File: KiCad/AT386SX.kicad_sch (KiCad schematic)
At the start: 31 parts, among them Q3 2N3904, U2 74HC05, U7 Cx486SLC, U8 80387SX, U9 RC2016A5, X1 CPU_CLK, X2 FPU_CLK, Y1 14.31818MHz

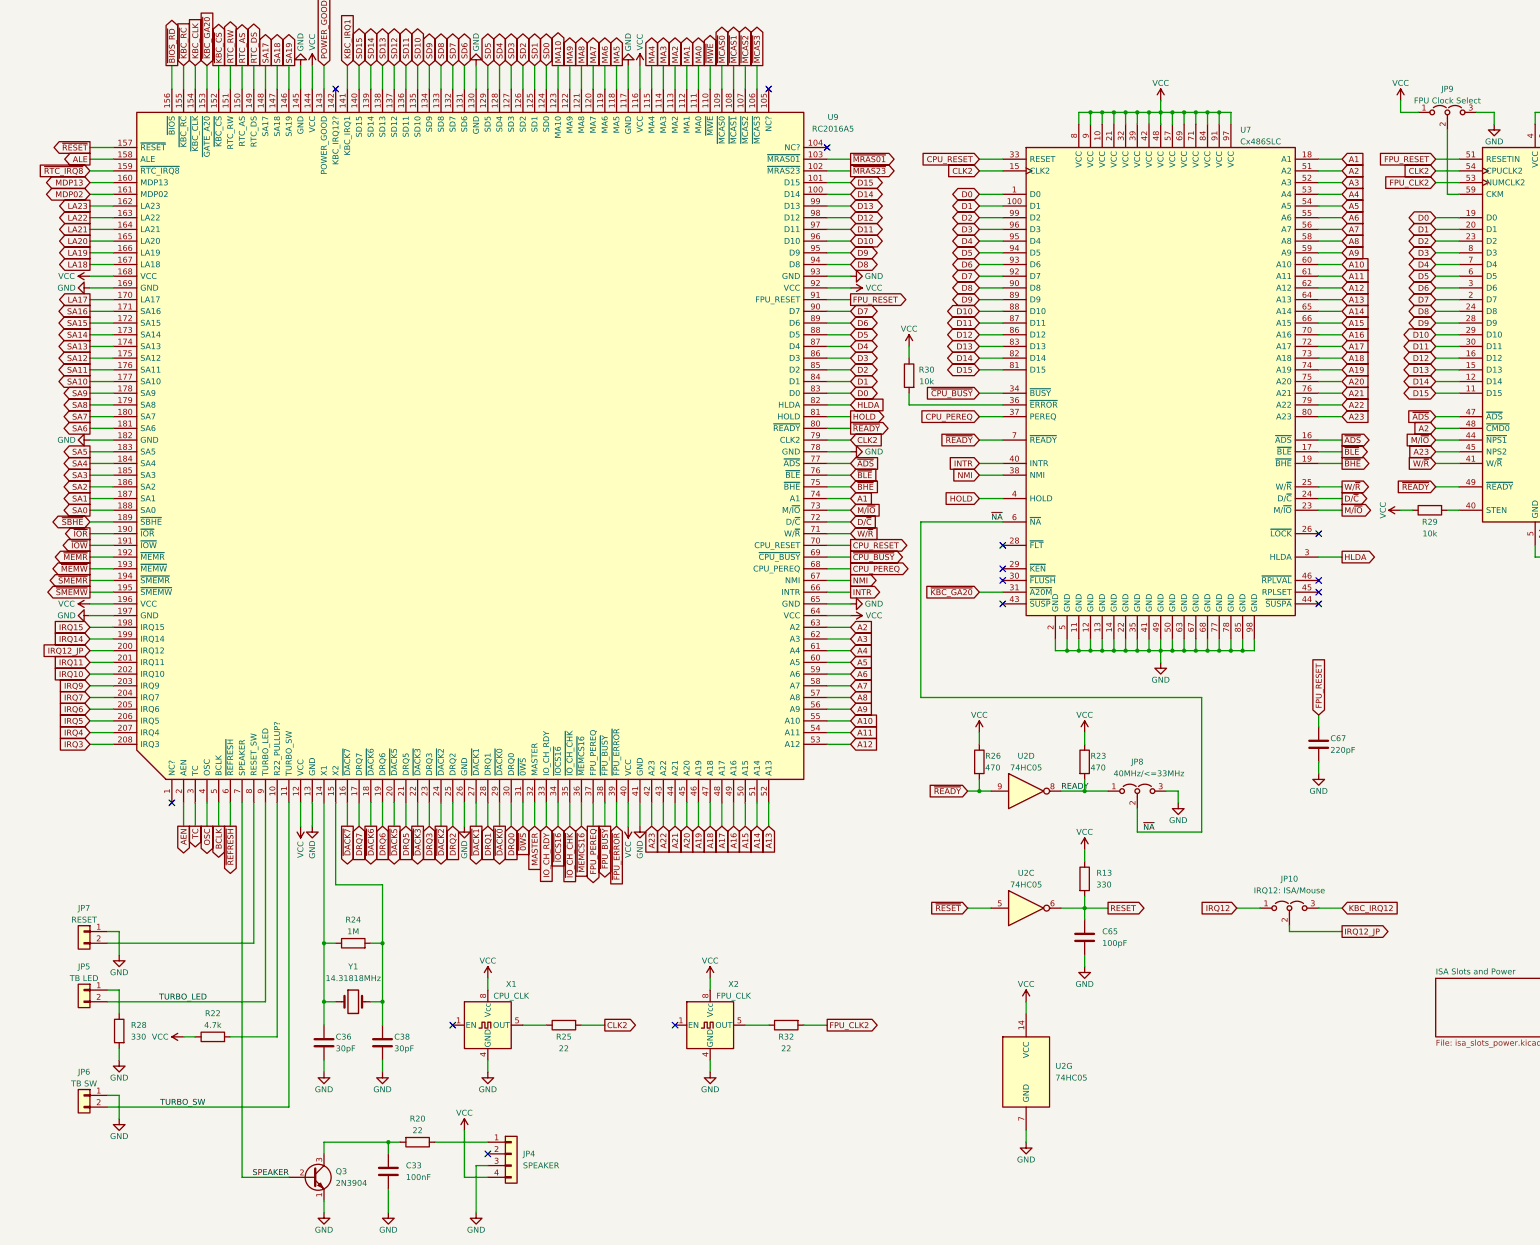
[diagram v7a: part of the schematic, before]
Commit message: Version 1.7: Use single front panel connector
Signed-off-by: Sergey Kiselev <skiselev@gmail.com>
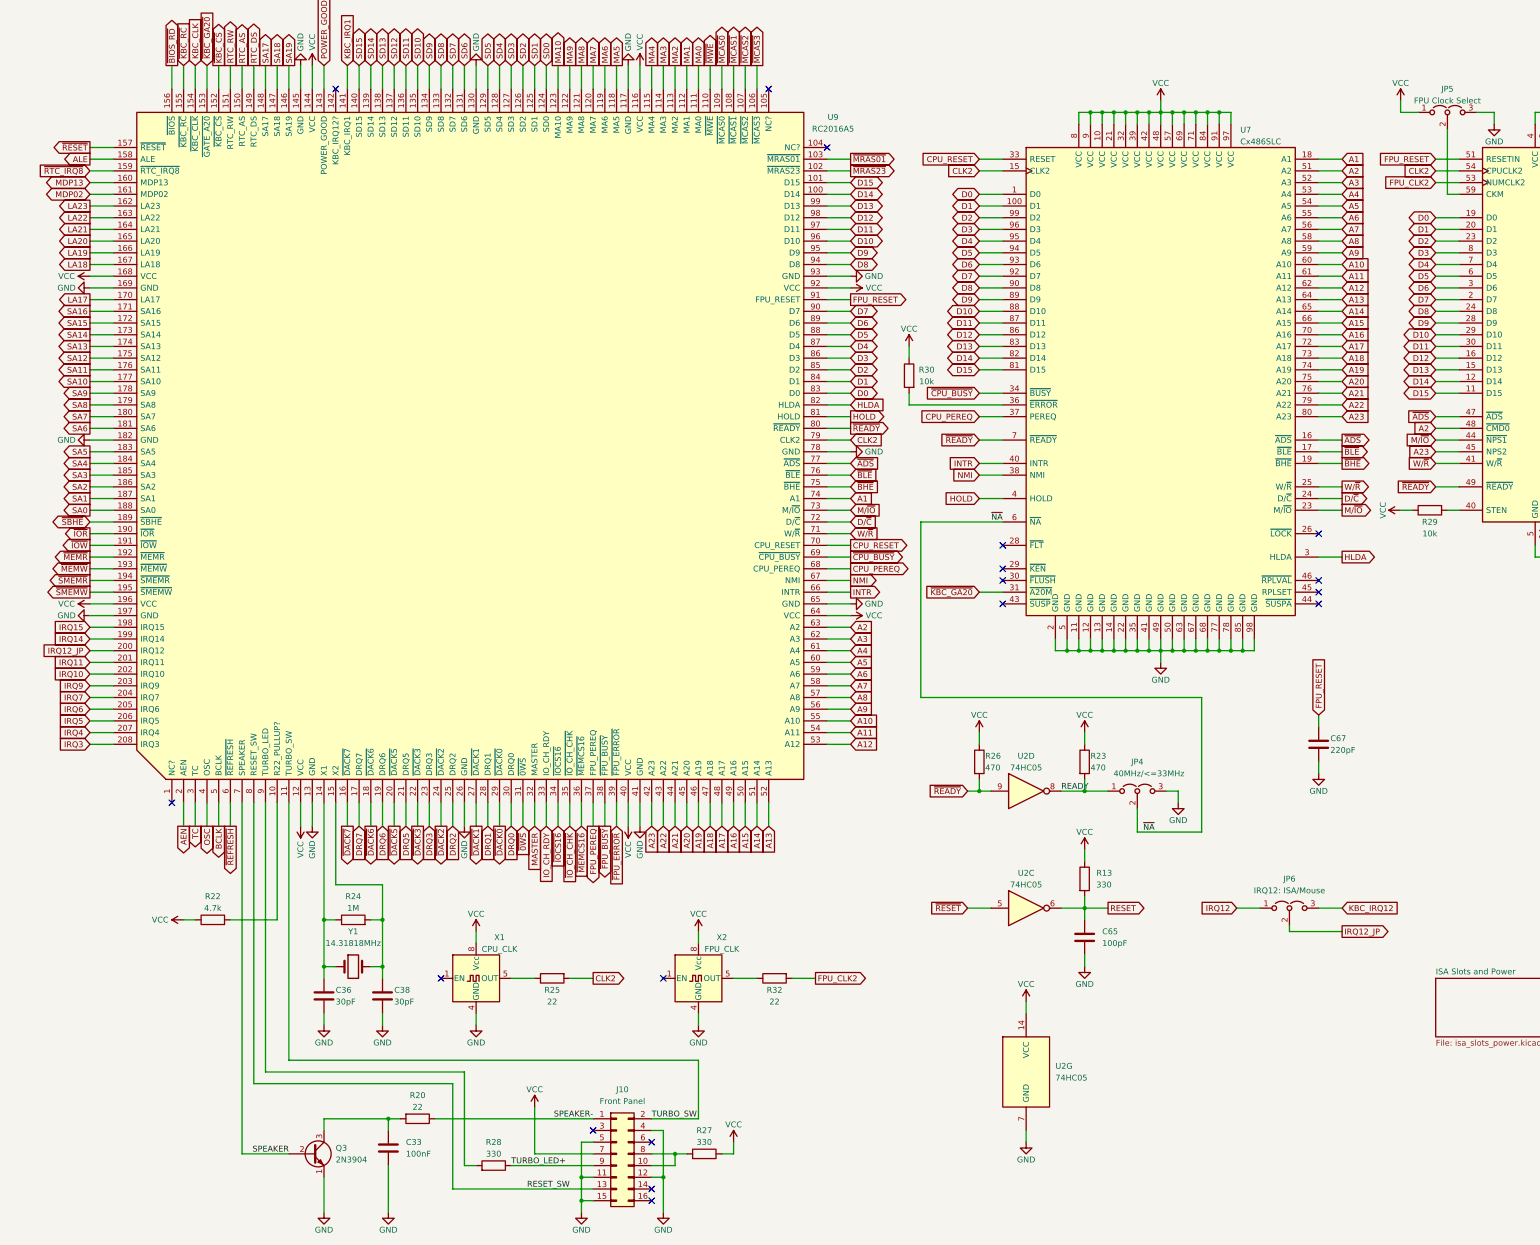
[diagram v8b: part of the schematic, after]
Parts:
- removed JP4: SPEAKER, My_Components:Conn_Pin_Header_4x1_2.54mm, symbol Connector_Generic:Conn_01x04
- removed JP5: TB LED, My_Components:Conn_Pin_Header_2x1_2.54mm, symbol Connector_Generic:Conn_01x02
- removed JP6: TB SW, My_Components:Conn_Pin_Header_2x1_2.54mm, symbol Connector_Generic:Conn_01x02
- removed JP7: RESET, My_Components:Conn_Pin_Header_2x1_2.54mm, symbol Connector_Generic:Conn_01x02
- added J10: Front Panel, My_Components:Conn_Pin_Header_8x2_2.54mm, symbol Connector_Generic:Conn_02x08_Odd_Even
- added R27: 330, My_Components:Res_762, symbol Device:R
- renumbered JP8 to JP4, JP9 to JP5, JP10 to JP6
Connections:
- net GND: now also J10.11 (Pin_11), J10.12 (Pin_12), J10.15 (Pin_15), J10.4 (Pin_4), J10.5 (Pin_5); no longer R28.2
- net TURBO_SW: now also J10.2 (Pin_2)
- net VCC: now also J10.7 (Pin_7), R27.1
- net SPEAKER-: now reaches R20.1
- net SPEAKER-: now also J10.1 (Pin_1)
- net RESET_SW: now reaches U9.8 (RESET_SW)
- net RESET_SW: now also J10.13 (Pin_13)
- net TURBO_LED+: now reaches R28.1
- net TURBO_LED+: now also J10.9 (Pin_9)
- net TURBO_LED: no longer names the net of U9.9 (TURBO_LED)
- net TURBO_LED: now also R28.2
- new net: J10.10 (Pin_10), J10.8 (Pin_8), R27.2
- no-connect marks 16 -> 19
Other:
- moved on the sheet: C33, C36, C38, Q3, R20, R22, R24, R25, R28, R32, X1, X2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
